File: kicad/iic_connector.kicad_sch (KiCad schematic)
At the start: 15 parts

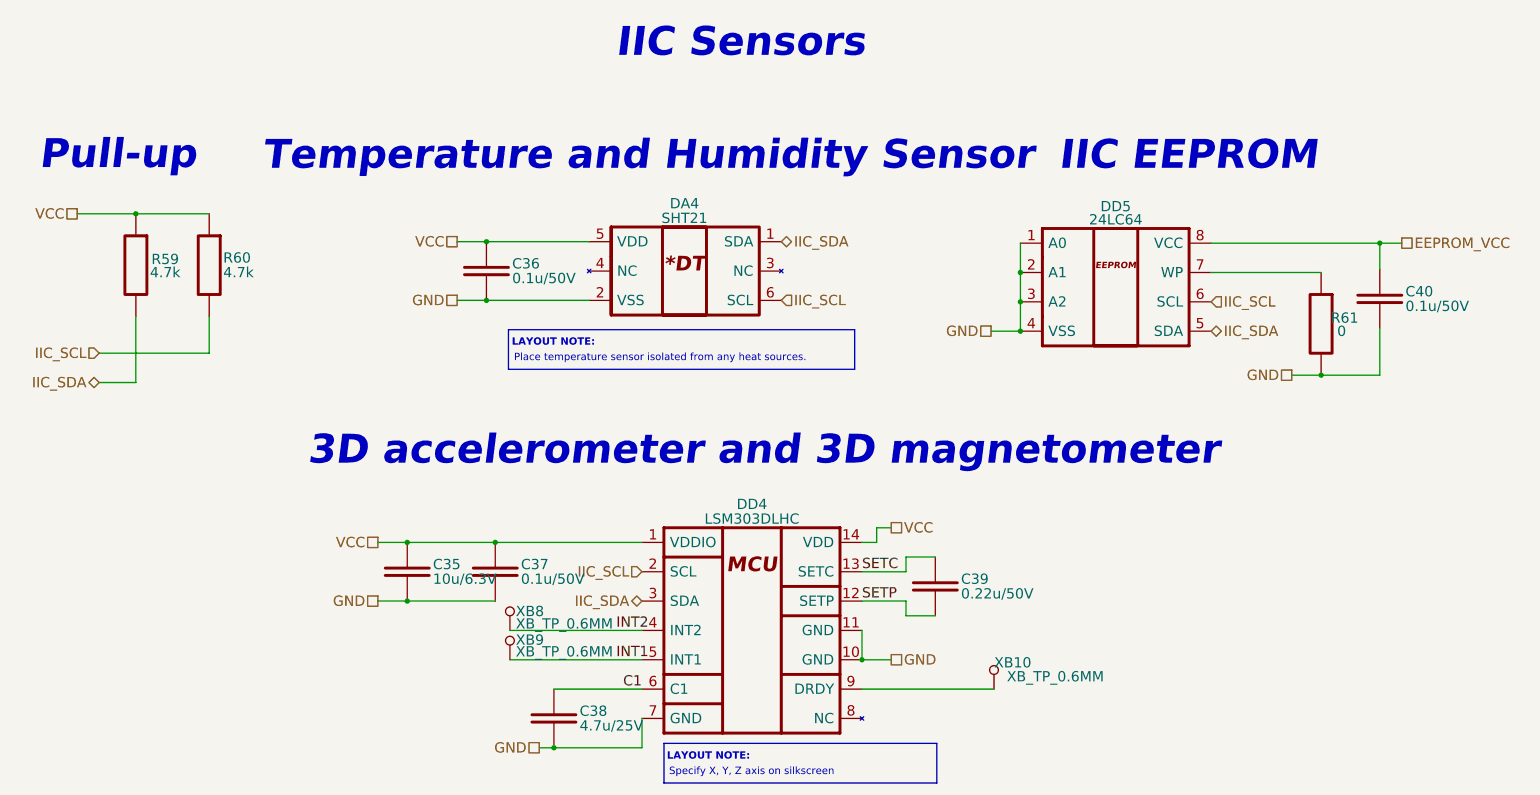
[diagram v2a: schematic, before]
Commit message: Add docs; Update values of components according to PCB
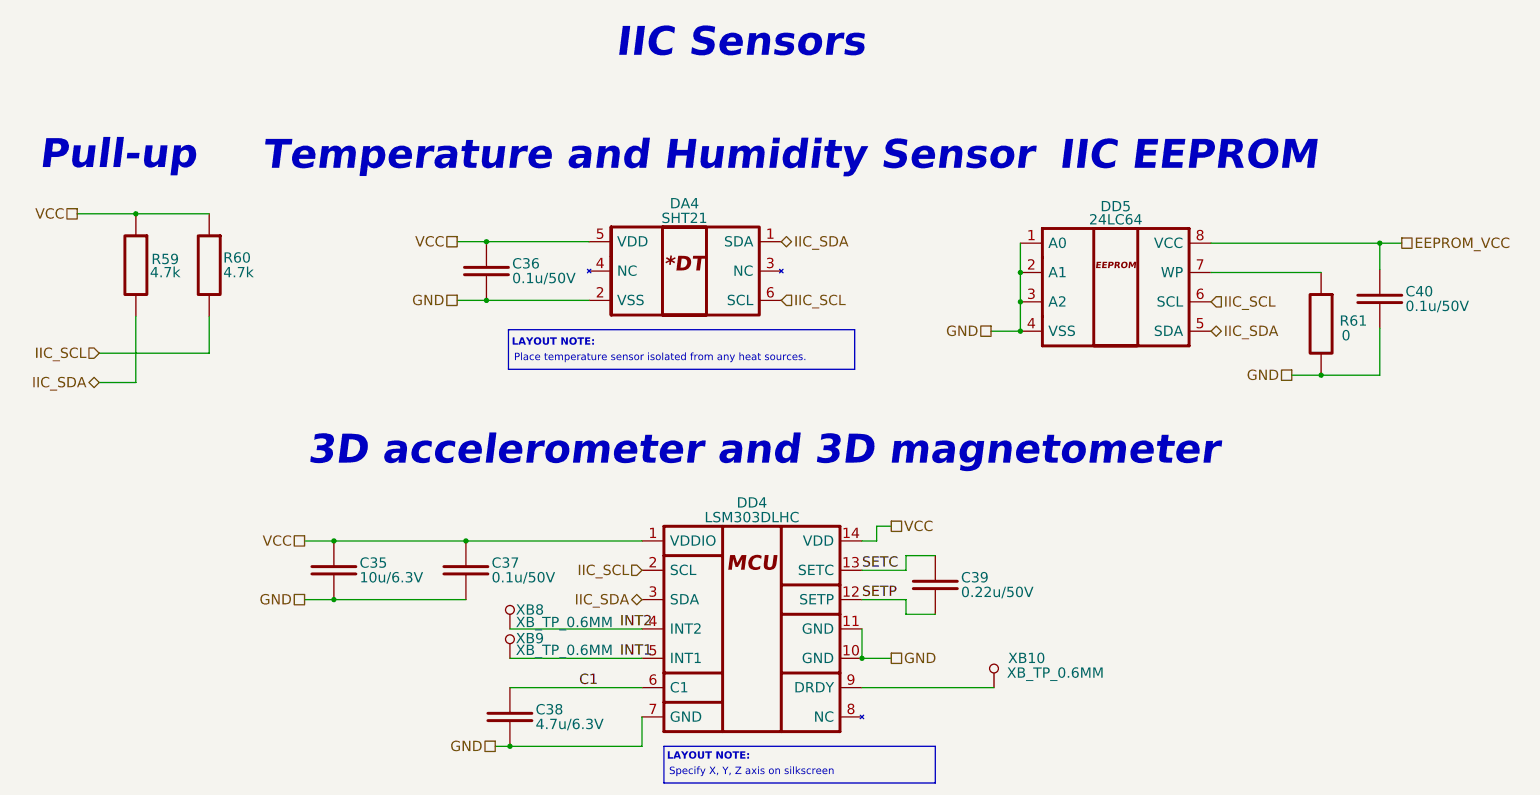
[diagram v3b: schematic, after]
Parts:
- C38: value 4.7u/25V -> 4.7u/6.3V
- DD5: Assembly DNP -> (none)
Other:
- moved on the sheet: C35, C37, C38

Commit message: Add wiring diagram; Add work ours (stage 2); refactor folders
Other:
- title: (none) -> RadioSens v1
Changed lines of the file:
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@@
 (kicad_sch (version 20211123) (generator eeschema)
   (paper "A4")
+  (title_block
+    (title "RadioSens v1")
+    (comment 2 "Electrical Circuit")
+  )
   (junction (at 261.112 70.358) (diameter 0) (color 0 0 0 0)
   )
